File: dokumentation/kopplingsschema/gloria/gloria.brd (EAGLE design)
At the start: 100 x 80.1 mm, 27 parts, among them IC1 74LS125N

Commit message: Routed board!
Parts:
- moved C3 2.01 mm to (50.2, 59.7)
- moved C9 2.01 mm to (50.2, 54.6)
- moved R1 2.01 mm to (50.2, 57.1)
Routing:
- net RESET: track 207.1 -> 128.2 mm, vias 2 -> 1
- net N$33: track 89.5 -> 56.9 mm, vias 2 -> 0
- net GND: track 19.7 -> 0.00 mm, vias 3 -> 0
- net N$12: track 37.6 -> 18.0 mm
- net LINEVALUE: track 52.3 -> 68.7 mm
- net N$42: track 78.3 -> 64.4 mm
- net LINEADDR1: track 47.2 -> 59.9 mm, vias 0 -> 1
- net VCC: track 327.0 -> 337.9 mm, vias 2 -> 3
- net N$21: track 35.9 -> 26.0 mm
- net N$37: track 11.1 -> 18.8 mm, vias 0 -> 1
- net N$11: track 22.8 -> 15.4 mm, vias 1 -> 0
- net N$13: track 15.4 -> 22.5 mm
- net MISO: track 64.0 -> 69.9 mm, vias 3 -> 0
- net N$36: track 17.0 -> 22.0 mm, vias 0 -> 1
- net SCK: track 87.0 -> 82.1 mm
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
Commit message: Connected uninvoked pins.
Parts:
- ATMEGA1284P: value (none) -> SENSOR UNIT
- ATMEGA1284P1: value (none) -> DRIVE UNIT
- Q1, Q2: value (none) -> 16M
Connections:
- removed net VDD: LINEENABLEMUX1.24, LINEVALUEMUX1.24
- removed net VSS: LINEENABLEMUX1.12, LINEVALUEMUX1.12
- net GND: now also LINEENABLEMUX1.12, LINEVALUEMUX1.12
- net VCC: now also LINEENABLEMUX1.24, LINEVALUEMUX1.24
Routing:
- net VSS: track 39.7 -> 0.00 mm, vias 2 -> 0
- net VDD: track 29.6 -> 0.00 mm
- net VCC: track 337.9 -> 366.5 mm
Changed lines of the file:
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@@
 </autorouter>
 <elements>
-<element name="ATMEGA1284P" library="1284p" package="DIL40" value="" x="48.26" y="26.67" rot="R270"/>
+<element name="ATMEGA1284P" library="1284p" package="DIL40" value="SENSOR UNIT" x="48.26" y="26.67" rot="R270"/>
 <element name="LINEVALUEMUX1" library="40xx" package="DIL24-6" value="4067N" x="82.55" y="39.37" rot="R180"/>
 <element name="LINEENABLEMUX1" library="40xx" package="DIL24-6" value="4067N" x="82.55" y="10.795" rot="R180"/>
-<element name="ATMEGA1284P1" library="1284p" package="DIL40" value="" x="10.668" y="26.67" rot="R270"/>
+<element name="ATMEGA1284P1" library="1284p" package="DIL40" value="DRIVE UNIT" x="10.668" y="26.67" rot="R270"/>
 <element name="IC1" library="74xx-eu" package="DIL14" value="74LS125N" x="11.43" y="71.12"/>
 <element name="SENSOR_DISTANCE_1" library="con-molex" package="22-23-2031" value="22-23-2031" x="62.865" y="10.795" rot="R90">
@@
 <attribute name="OC_FARNELL" value="unknown" x="-55.88" y="-19.05" size="1.778" layer="27" rot="R270" display="off"/>
 </element>
-<element name="Q1" library="special" package="QS" value="" x="34.925" y="28.575" rot="R90"/>
-<element name="Q2" library="special" package="QS" value="" x="23.495" y="28.575" rot="R90"/>
+<element name="Q1" library="special" package="QS" value="16M" x="34.925" y="28.575" rot="R90"/>
+<element name="Q2" library="special" package="QS" value="16M" x="23.495" y="28.575" rot="R90"/>
 <element name="C9" library="rcl" package="C025-024X044" value="100n" x="50.165" y="54.61"/>
 <element name="C11" library="rcl" package="C025-024X044" value="22p" x="29.21" y="27.305"/>
@@
 </elements>
 <signals>
-<signal name="VSS">
-<contactref element="LINEVALUEMUX1" pad="12"/>
-<contactref element="LINEENABLEMUX1" pad="12"/>
-<wire x1="64.77" y1="19.05" x2="68.58" y2="19.05" width="0.254" layer="16"/>
-<wire x1="59.69" y1="24.13" x2="64.77" y2="19.05" width="0.254" layer="1"/>
-<wire x1="59.69" y1="29.21" x2="59.69" y2="24.13" width="0.254" layer="1"/>
-<wire x1="66.04" y1="35.56" x2="59.69" y2="29.21" width="0.254" layer="1"/>
-<wire x1="66.04" y1="44.45" x2="66.04" y2="35.56" width="0.254" layer="1"/>
-<wire x1="66.04" y1="46.99" x2="66.04" y2="44.45" width="0.254" layer="16"/>
-<wire x1="68.58" y1="46.99" x2="66.04" y2="46.99" width="0.254" layer="16"/>
-<wire x1="68.58" y1="19.05" x2="68.58" y2="18.415" width="0.254" layer="16"/>
-<via x="64.77" y="19.05" extent="1-16" drill="0.6096"/>
-<via x="66.04" y="44.45" extent="1-16" drill="0.6096"/>
-</signal>
-<signal name="VDD">
-<contactref element="LINEVALUEMUX1" pad="24"/>
-<contactref element="LINEENABLEMUX1" pad="24"/>
-<wire x1="97.79" y1="5.08" x2="96.52" y2="3.81" width="0.254" layer="1"/>
-<wire x1="97.79" y1="29.21" x2="97.79" y2="5.08" width="0.254" layer="1"/>
-<wire x1="96.52" y1="30.48" x2="97.79" y2="29.21" width="0.254" layer="1"/>
-<wire x1="96.52" y1="31.75" x2="96.52" y2="30.48" width="0.254" layer="1"/>
-<wire x1="96.52" y1="3.81" x2="96.52" y2="3.175" width="0.254" layer="1"/>
-</signal>
 <signal name="GND">
 <contactref element="IC1" pad="7"/>
@@
 <contactref element="JP1" pad="GND@2"/>
 <contactref element="JP1" pad="GND@1"/>
+<contactref element="LINEENABLEMUX1" pad="12"/>
+<contactref element="LINEVALUEMUX1" pad="12"/>
+<contactref element="IC1" pad="7"/>
+<wire x1="34.29" y1="53.34" x2="33.88998125" y2="53.287796875" width="0.254" layer="1"/>
+<wire x1="33.89" y1="54.045" x2="33.89" y2="63.57" width="0" layer="19" extent="1-1"/>
 </signal>
 <signal name="VCC">
@@
 <via x="43.18" y="67.945" extent="1-16" drill="0.6"/>
 <wire x1="43.18" y1="67.945" x2="44.45" y2="67.945" width="0.4064" layer="1"/>
+<contactref element="LINEVALUEMUX1" pad="24"/>
+<wire x1="96.52" y1="18.415" x2="96.52" y2="31.75" width="0.254" layer="1"/>
+<contactref element="LINEENABLEMUX1" pad="24"/>
+<contactref element="IC1" pad="14"/>
+<wire x1="96.52" y1="18.415" x2="96.52" y2="3.175" width="0.254" layer="1"/>
 </signal>
 <signal name="LINEADDR0">

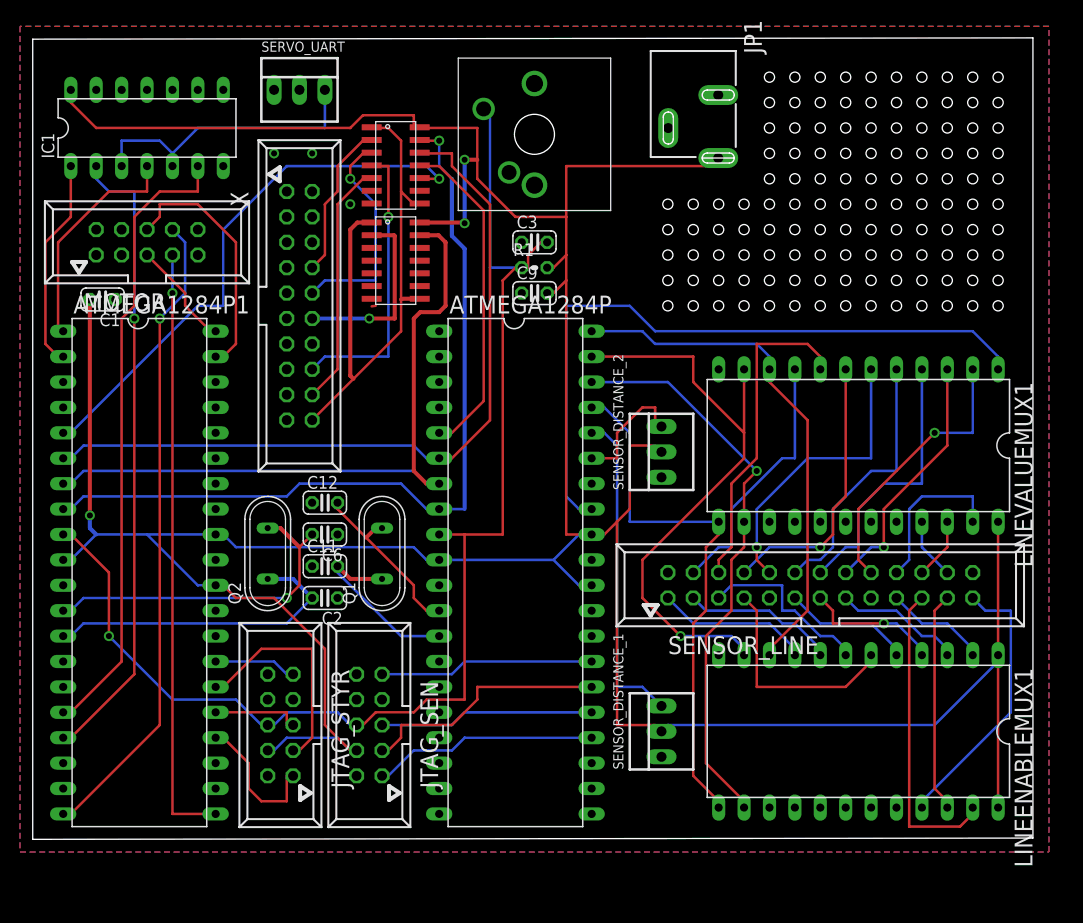
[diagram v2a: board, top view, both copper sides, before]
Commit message: Added prototyping area.
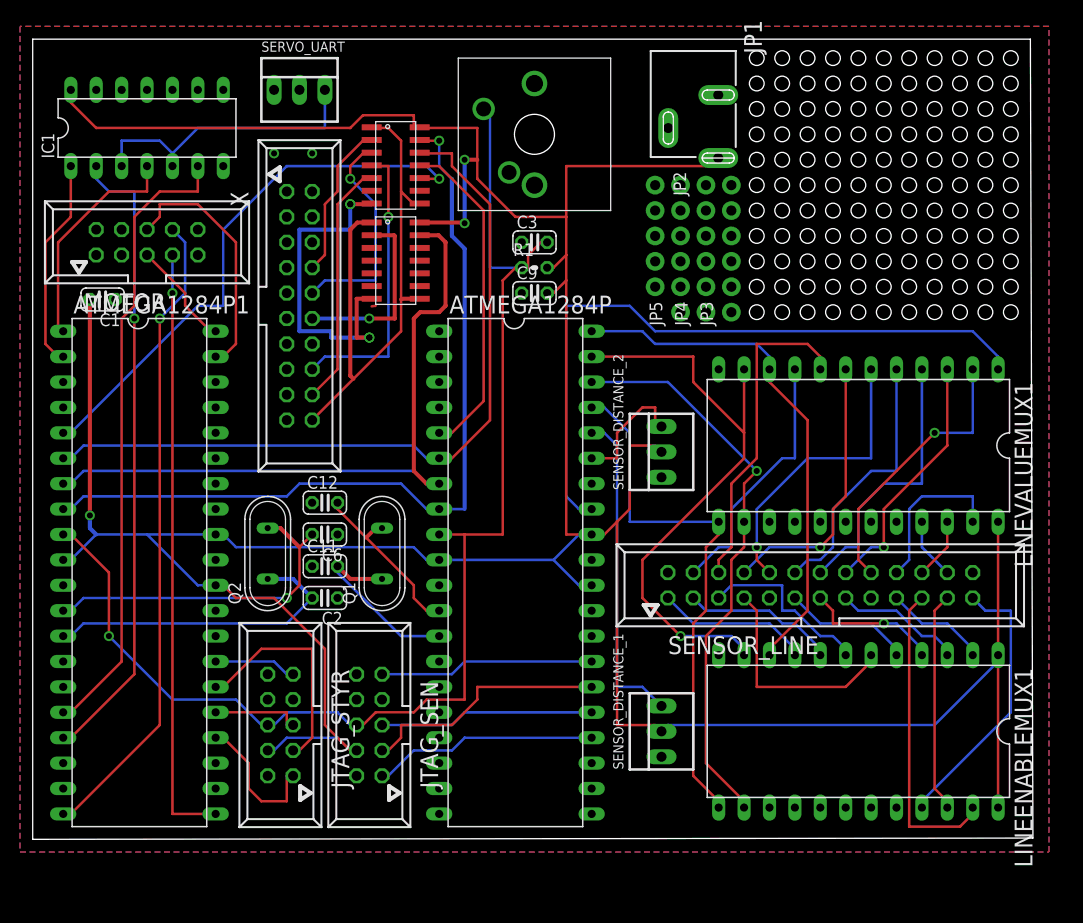
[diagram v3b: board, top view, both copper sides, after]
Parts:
- added JP2: (no value), SparkFun-Connectors:1X05_NO_SILK
- added JP26, JP27, JP28, JP29, JP30, JP31, JP32, JP33, JP34, JP35, JP36: M11POGOPIN_HOLES_ONLY, SparkFun-Connectors:1X11_HOLES_ONLY
- added JP3, JP4, JP5: (no value), SparkFun-Connectors:1X06_NO_SILK
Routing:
- net GND: track 0.40 -> 34.7 mm, vias 0 -> 2
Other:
- board size 100 x 80.1 mm -> 100 x 80 mm
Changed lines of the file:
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@@
 <plain>
 <wire x1="0" y1="0" x2="100" y2="0.127" width="0" layer="20"/>
-<wire x1="100" y1="0.127" x2="99.9998" y2="80.127" width="0" layer="20"/>
-<wire x1="99.9998" y1="80.127" x2="0" y2="79.999840625" width="0" layer="20"/>
+<wire x1="100" y1="0.127" x2="99.7458" y2="80" width="0" layer="20"/>
+<wire x1="99.7458" y1="80" x2="0" y2="79.999840625" width="0" layer="20"/>
 <wire x1="0" y1="79.999840625" x2="0" y2="0" width="0" layer="20"/>
-<hole x="71.12" y="53.34" drill="1.016"/>
-<hole x="73.66" y="53.34" drill="1.016"/>
-<hole x="76.2" y="53.34" drill="1.016"/>
-<hole x="78.74" y="53.34" drill="1.016"/>
-<hole x="81.28" y="53.34" drill="1.016"/>
-<hole x="86.36" y="53.34" drill="1.016"/>
-<hole x="83.82" y="53.34" drill="1.016"/>
-<hole x="88.9" y="53.34" drill="1.016"/>
-<hole x="91.44" y="53.34" drill="1.016"/>
-<hole x="93.98" y="53.34" drill="1.016"/>
-<hole x="96.52" y="53.34" drill="1.016"/>
-<hole x="96.52" y="55.88" drill="1.016"/>
-<hole x="93.98" y="55.88" drill="1.016"/>
-<hole x="91.44" y="55.88" drill="1.016"/>
-<hole x="88.9" y="55.88" drill="1.016"/>
-<hole x="86.36" y="55.88" drill="1.016"/>
-<hole x="83.82" y="55.88" drill="1.016"/>
-<hole x="81.28" y="55.88" drill="1.016"/>
-<hole x="78.74" y="55.88" drill="1.016"/>
-<hole x="76.2" y="55.88" drill="1.016"/>
-<hole x="73.66" y="55.88" drill="1.016"/>
-<hole x="71.12" y="55.88" drill="1.016"/>
-<hole x="71.12" y="58.42" drill="1.016"/>
-<hole x="73.66" y="58.42" drill="1.016"/>
-<hole x="76.2" y="58.42" drill="1.016"/>
-<hole x="78.74" y="58.42" drill="1.016"/>
-<hole x="81.28" y="58.42" drill="1.016"/>
-<hole x="83.82" y="58.42" drill="1.016"/>
-<hole x="86.36" y="58.42" drill="1.016"/>
-<hole x="88.9" y="58.42" drill="1.016"/>
-<hole x="91.44" y="58.42" drill="1.016"/>
-<hole x="93.98" y="58.42" drill="1.016"/>
-<hole x="96.52" y="58.42" drill="1.016"/>
-<hole x="96.52" y="60.96" drill="1.016"/>
-<hole x="93.98" y="60.96" drill="1.016"/>
-<hole x="91.44" y="60.96" drill="1.016"/>
-<hole x="88.9" y="60.96" drill="1.016"/>
-<hole x="86.36" y="60.96" drill="1.016"/>
-<hole x="83.82" y="60.96" drill="1.016"/>
-<hole x="81.28" y="60.96" drill="1.016"/>
-<hole x="78.74" y="60.96" drill="1.016"/>
-<hole x="76.2" y="60.96" drill="1.016"/>
-<hole x="73.66" y="60.96" drill="1.016"/>
-<hole x="71.12" y="60.96" drill="1.016"/>
-<hole x="71.12" y="63.5" drill="1.016"/>
-<hole x="73.66" y="63.5" drill="1.016"/>
-<hole x="76.2" y="63.5" drill="1.016"/>
-<hole x="78.74" y="63.5" drill="1.016"/>
-<hole x="81.28" y="63.5" drill="1.016"/>
-<hole x="83.82" y="63.5" drill="1.016"/>
-<hole x="86.36" y="63.5" drill="1.016"/>
-<hole x="88.9" y="63.5" drill="1.016"/>
-<hole x="91.44" y="63.5" drill="1.016"/>
-<hole x="93.98" y="63.5" drill="1.016"/>
-<hole x="96.52" y="63.5" drill="1.016"/>
-<hole x="96.52" y="66.04" drill="1.016"/>
-<hole x="93.98" y="66.04" drill="1.016"/>
-<hole x="91.44" y="66.04" drill="1.016"/>
-<hole x="88.9" y="66.04" drill="1.016"/>
-<hole x="83.82" y="66.04" drill="1.016"/>
-<hole x="86.36" y="66.04" drill="1.016"/>
-<hole x="81.28" y="66.04" drill="1.016"/>
-<hole x="78.74" y="66.04" drill="1.016"/>
-<hole x="76.2" y="66.04" drill="1.016"/>
-<hole x="73.66" y="66.04" drill="1.016"/>
-<hole x="73.66" y="68.58" drill="1.016"/>
-<hole x="73.66" y="71.12" drill="1.016"/>
-<hole x="73.66" y="73.66" drill="1.016"/>
-<hole x="76.2" y="73.66" drill="1.016"/>
-<hole x="76.2" y="71.12" drill="1.016"/>
-<hole x="76.2" y="68.58" drill="1.016"/>
-<hole x="78.74" y="68.58" drill="1.016"/>
-<hole x="78.74" y="71.12" drill="1.016"/>
-<hole x="78.74" y="73.66" drill="1.016"/>
-<hole x="81.28" y="73.66" drill="1.016"/>
-<hole x="81.28" y="71.12" drill="1.016"/>
-<hole x="81.28" y="68.58" drill="1.016"/>
-<hole x="83.82" y="68.58" drill="1.016"/>
-<hole x="83.82" y="71.12" drill="1.016"/>
-<hole x="83.82" y="73.66" drill="1.016"/>
-<hole x="86.36" y="73.66" drill="1.016"/>
-<hole x="86.36" y="71.12" drill="1.016"/>
-<hole x="86.36" y="68.58" drill="1.016"/>
-<hole x="88.9" y="68.58" drill="1.016"/>
-<hole x="88.9" y="71.12" drill="1.016"/>
-<hole x="88.9" y="73.66" drill="1.016"/>
-<hole x="91.44" y="73.66" drill="1.016"/>
-<hole x="91.44" y="71.12" drill="1.016"/>
-<hole x="91.44" y="68.58" drill="1.016"/>
-<hole x="93.98" y="68.58" drill="1.016"/>
-<hole x="93.98" y="71.12" drill="1.016"/>
-<hole x="93.98" y="73.66" drill="1.016"/>
-<hole x="73.66" y="76.2" drill="1.016"/>
-<hole x="76.2" y="76.2" drill="1.016"/>
-<hole x="78.74" y="76.2" drill="1.016"/>
-<hole x="81.28" y="76.2" drill="1.016"/>
-<hole x="83.82" y="76.2" drill="1.016"/>
-<hole x="86.36" y="76.2" drill="1.016"/>
-<hole x="88.9" y="76.2" drill="1.016"/>
-<hole x="91.44" y="76.2" drill="1.016"/>
-<hole x="93.98" y="76.2" drill="1.016"/>
-<hole x="96.52" y="76.2" drill="1.016"/>
-<hole x="96.52" y="73.66" drill="1.016"/>
-<hole x="96.52" y="71.12" drill="1.016"/>
-<hole x="96.52" y="68.58" drill="1.016"/>
-<hole x="68.58" y="63.5" drill="1.016"/>
-<hole x="66.04" y="63.5" drill="1.016"/>
-<hole x="63.5" y="63.5" drill="1.016"/>
-<hole x="63.5" y="60.96" drill="1.016"/>
-<hole x="66.04" y="60.96" drill="1.016"/>
-<hole x="68.58" y="60.96" drill="1.016"/>
-<hole x="68.58" y="58.42" drill="1.016"/>
-<hole x="66.04" y="58.42" drill="1.016"/>
-<hole x="63.5" y="58.42" drill="1.016"/>
-<hole x="63.5" y="55.88" drill="1.016"/>
-<hole x="66.04" y="55.88" drill="1.016"/>
-<hole x="68.58" y="55.88" drill="1.016"/>
-<hole x="68.58" y="53.34" drill="1.016"/>
-<hole x="66.04" y="53.34" drill="1.016"/>
-<hole x="63.5" y="53.34" drill="1.016"/>
 </plain>
 <attributes>
@@
 <attribute name="PROD_ID" value="PRT-00119" x="71.12" y="81.915" size="1.778" layer="27" rot="R180" display="off"/>
 </element>
+<element name="JP26" library="SparkFun-Connectors" package="1X11_HOLES_ONLY" value="M11POGOPIN_HOLES_ONLY" x="72.39" y="78.105"/>
+<element name="JP27" library="SparkFun-Connectors" package="1X11_HOLES_ONLY" value="M11POGOPIN_HOLES_ONLY" x="72.39" y="75.565"/>
+<element name="JP28" library="SparkFun-Connectors" package="1X11_HOLES_ONLY" value="M11POGOPIN_HOLES_ONLY" x="72.39" y="73.025"/>
+<element name="JP29" library="SparkFun-Connectors" package="1X11_HOLES_ONLY" value="M11POGOPIN_HOLES_ONLY" x="72.39" y="70.485"/>
+<element name="JP30" library="SparkFun-Connectors" package="1X11_HOLES_ONLY" value="M11POGOPIN_HOLES_ONLY" x="72.39" y="67.945"/>
+<element name="JP31" library="SparkFun-Connectors" package="1X11_HOLES_ONLY" value="M11POGOPIN_HOLES_ONLY" x="72.39" y="65.405"/>
+<element name="JP32" library="SparkFun-Connectors" package="1X11_HOLES_ONLY" value="M11POGOPIN_HOLES_ONLY" x="72.39" y="62.865"/>
+<element name="JP33" library="SparkFun-Connectors" package="1X11_HOLES_ONLY" value="M11POGOPIN_HOLES_ONLY" x="72.39" y="60.325"/>
+<element name="JP34" library="SparkFun-Connectors" package="1X11_HOLES_ONLY" value="M11POGOPIN_HOLES_ONLY" x="72.39" y="57.785"/>
+<element name="JP35" library="SparkFun-Connectors" package="1X11_HOLES_ONLY" value="M11POGOPIN_HOLES_ONLY" x="72.39" y="55.245"/>
+<element name="JP36" library="SparkFun-Connectors" package="1X11_HOLES_ONLY" value="M11POGOPIN_HOLES_ONLY" x="72.39" y="52.705"/>
+<element name="JP3" library="SparkFun-Connectors" package="1X06_NO_SILK" value="" x="69.85" y="52.705" rot="R90">
+<attribute name="PROD_ID" value="CONN-08437" x="69.85" y="52.705" size="1.778" layer="27" rot="R90" display="off"/>
+</element>
+<element name="JP4" library="SparkFun-Connectors" package="1X06_NO_SILK" value="" x="67.31" y="52.705" rot="R90">
+<attribute name="PROD_ID" value="CONN-08437" x="67.31" y="52.705" size="1.778" layer="27" rot="R90" display="off"/>
+</element>
+<element name="JP5" library="SparkFun-Connectors" package="1X06_NO_SILK" value="" x="64.77" y="52.705" rot="R90">
+<attribute name="PROD_ID" value="CONN-08437" x="64.77" y="52.705" size="1.778" layer="27" rot="R90" display="off"/>
+</element>
+<element name="JP2" library="SparkFun-Connectors" package="1X05_NO_SILK" value="" x="62.23" y="65.405" rot="R270"/>
 </elements>
 <signals>
@@
 <contactref element="IC1" pad="7"/>
 <wire x1="34.29" y1="53.34" x2="33.88998125" y2="53.287796875" width="0.254" layer="1"/>
-<wire x1="33.89" y1="54.045" x2="33.89" y2="63.57" width="0" layer="19" extent="1-1"/>
+<wire x1="33.89" y1="54.045" x2="32.385" y2="54.045" width="0.4064" layer="1"/>
+<wire x1="32.385" y1="54.045" x2="32.385" y2="50.165" width="0.4064" layer="1"/>
+<wire x1="32.385" y1="50.165" x2="33.655" y2="50.165" width="0.4064" layer="1"/>
+<via x="33.655" y="50.165" extent="1-16" drill="0.6"/>
+<wire x1="33.655" y1="50.165" x2="29.845" y2="50.165" width="0.4064" layer="16"/>
+<wire x1="29.845" y1="50.165" x2="29.845" y2="50.8" width="0.4064" layer="16"/>
+<wire x1="29.845" y1="50.8" x2="26.67" y2="50.8" width="0.4064" layer="16"/>
+<wire x1="26.67" y1="50.8" x2="26.67" y2="60.96" width="0.4064" layer="16"/>
+<wire x1="26.67" y1="60.96" x2="31.75" y2="60.96" width="0.4064" layer="16"/>
+<wire x1="31.75" y1="60.96" x2="31.75" y2="63.5" width="0.4064" layer="16"/>
+<via x="31.75" y="63.5" extent="1-16" drill="0.6"/>
+<wire x1="31.75" y1="63.5" x2="33.89" y2="63.5" width="0.4064" layer="1"/>
+<wire x1="33.89" y1="63.5" x2="33.89" y2="63.57" width="0.4064" layer="1"/>
 </signal>
 <signal name="VCC">
@@
 <via x="7.62" y="20.32" extent="1-16" drill="0.6096"/>
 </signal>
+<signal name="N$50">
+<via x="33.655" y="50.165" extent="1-16" drill="0.6"/>
+</signal>
 </signals>

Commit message: Rerouted board manually.
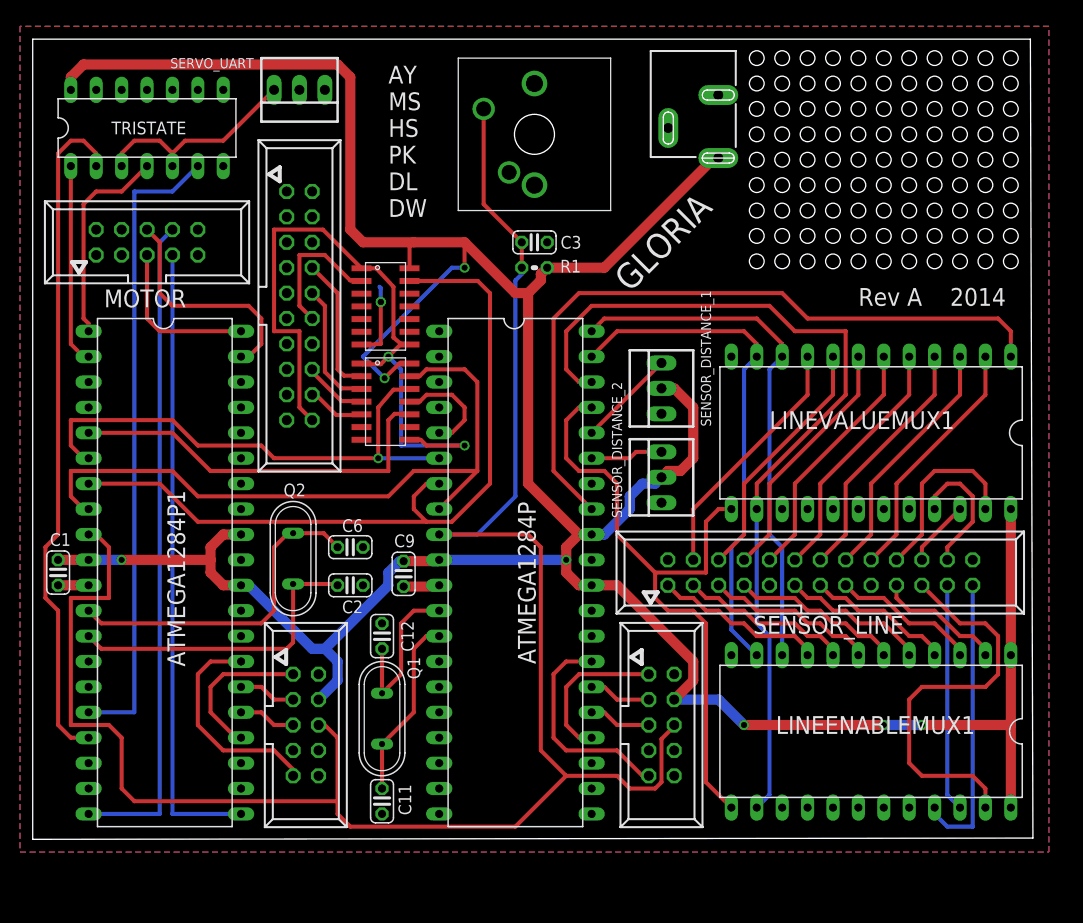
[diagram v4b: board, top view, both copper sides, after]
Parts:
- removed JP2: (no value), SparkFun-Connectors:1X05_NO_SILK
- removed JP3, JP4, JP5: (no value), SparkFun-Connectors:1X06_NO_SILK
- removed JP35, JP36: M11POGOPIN_HOLES_ONLY, SparkFun-Connectors:1X11_HOLES_ONLY
- moved SENSOR_DISTANCE_1 34.3 mm to (62.9, 45.1)
- moved C9 31.0 mm to (37.1, 26.5), turned to 90 degrees
- moved JTAG_SEN 29.2 mm to (62.9, 11.4), turned to 270 degrees
- moved C1 27.7 mm to (2.54, 26.7), turned to 90 degrees
- moved C11 24.2 mm to (34.9, 3.81), turned to 90 degrees
- moved U$1 23.6 mm to (33.3, 48.1)
- moved Q1 16.5 mm to (34.9, 12.1)
- moved C12 14.5 mm to (34.9, 20.3), turned to 270 degrees
- moved U$2 4.68 mm to (33.3, 57.7)
- moved C2 2.84 mm to (31.8, 25.4)
- moved C6 2.84 mm to (31.8, 29.2)
- moved Q2 2.59 mm to (26.0, 28.1)
- moved ATMEGA1284P1 2.54 mm to (13.2, 26.7)
- moved JTAG_STYR 2.54 mm to (27.3, 11.4), turned to 270 degrees
- moved SENSOR_DISTANCE_2 2.54 mm to (62.9, 36.2)
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- renumbered IC1 to TRISTATE
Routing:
- net RESET: track 128.2 -> 193.4 mm, vias 1 -> 0
- net VCC: track 366.5 -> 327.6 mm, vias 3 -> 7
- net LINEADDR2: track 57.5 -> 89.3 mm, vias 1 -> 0
- net MOSI: track 76.8 -> 52.3 mm, vias 0 -> 1
- net DISTANCELEFT: track 32.4 -> 9.88 mm
- net N$38: track 28.9 -> 6.42 mm, vias 1 -> 0
- net SS1: track 33.0 -> 10.7 mm
- net GND: track 34.7 -> 14.4 mm, vias 2 -> 1
- net N$3: track 25.1 -> 6.24 mm
- net N$39: track 24.6 -> 5.80 mm
- net N$7: track 22.6 -> 5.73 mm
- net SS0: track 55.6 -> 39.0 mm, vias 1 -> 0
- net N$4: track 21.5 -> 6.24 mm
- net N$33: track 56.9 -> 70.6 mm, vias 0 -> 2
- net N$6: track 8.27 -> 21.9 mm
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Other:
- board text added: "AY MS HS PK DL DW"
- board text added: "GLORIA"
- board text added: "Rev A 2014"
